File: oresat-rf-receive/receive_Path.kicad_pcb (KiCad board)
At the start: 4 copper layers, 26 x 60.3 mm, 32 parts, among them J1 Conn_Coaxial_142-0711-201, J2 0022232041, J3 0022232021, J5 0022232021, J6 Conn_Coaxial_142-0711-201, U1 TQP3M9037, U2 PAT1220-C-3DB, U3 SN74LVC1G32QDBVRQ1, U4 PAT1220-C-3DB, U5 TQP3M9037, U6 PD2328J5050S2HF, U7 LTC5505-1ES5

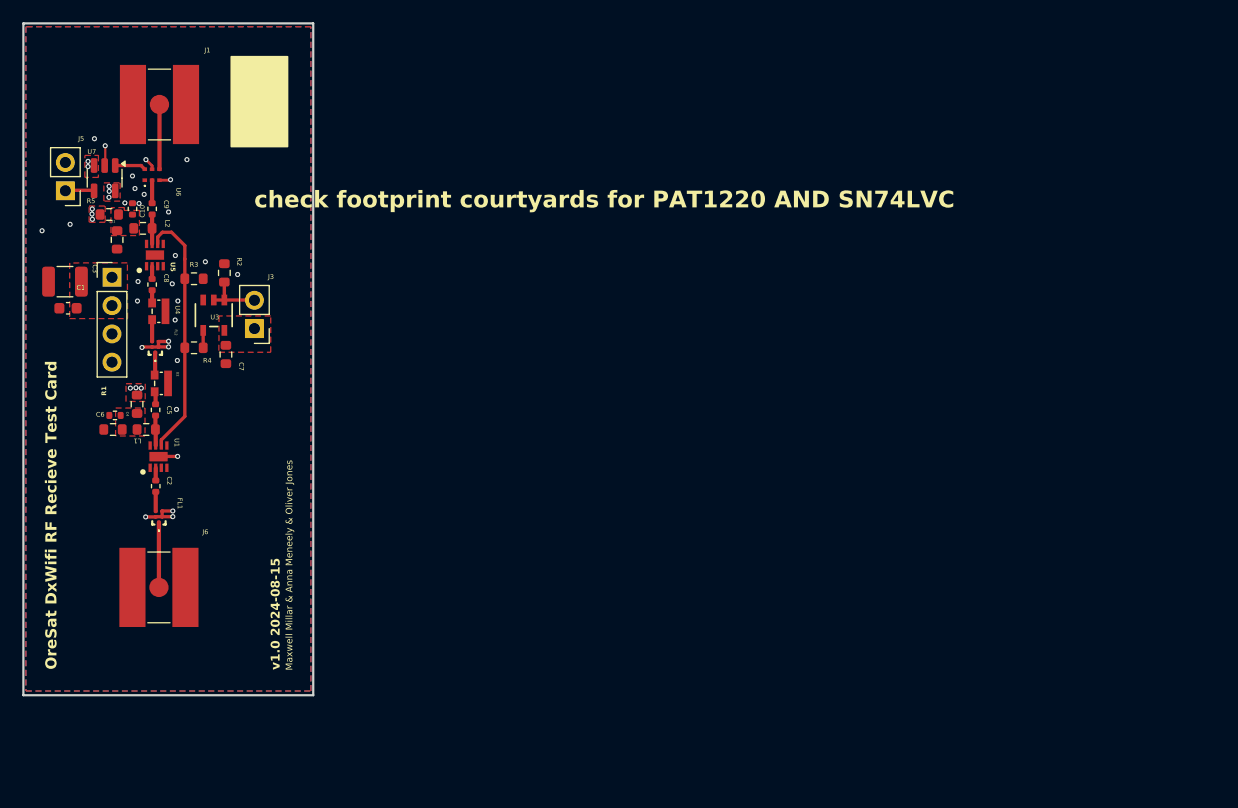
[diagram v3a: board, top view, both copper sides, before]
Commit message: 5V path changes and silkscreen descriptors update
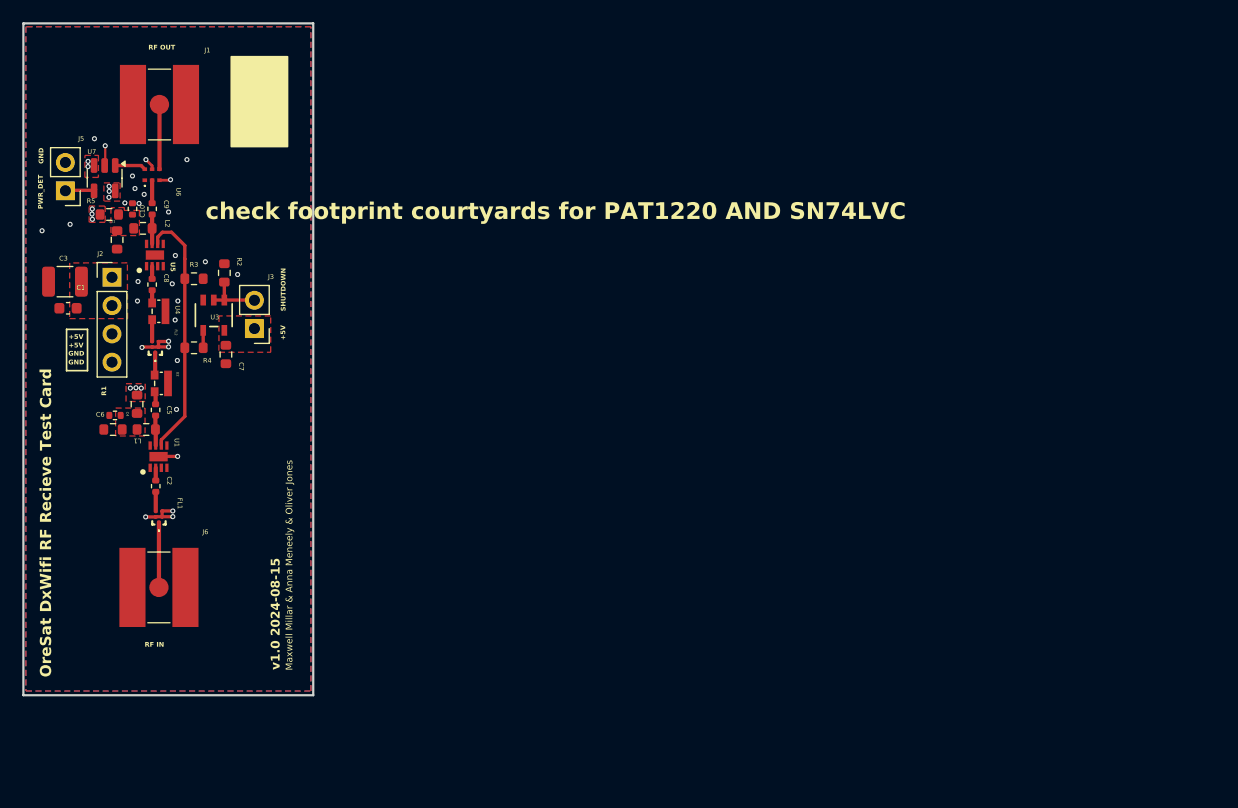
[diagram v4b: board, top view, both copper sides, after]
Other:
- board text added: "+5V"
- board text added: "GND"
- board text added: "PWR_DET"
- board text added: "RF IN"
- board text added: "RF OUT"
- board text added: "SHUTDOWN"
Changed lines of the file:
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@@
 		(tags "capacitor")
 		(property "Reference" "C3"
-			(at -2.69 1.1624 -90)
+			(at 0.1366 2.0928 0)
 			(unlocked yes)
 			(layer "F.SilkS")
@@
 		)
 		(property "Value" "22u"
-			(at 0 2.3 360)
+			(at 0 2.3 0)
 			(layer "F.Fab")
 			(hide yes)
@@
 		)
 		(property "Value" "2u2"
-			(at 0 1.43 360)
+			(at 0 1.43 0)
 			(layer "F.Fab")
 			(effects
@@
 		)
 		(fp_text user "${REFERENCE}"
-			(at 0 0 360)
+			(at 0 0 0)
 			(layer "F.Fab")
 			(effects
@@
 		(tags "Through hole pin header THT 1x04 2.54mm single row")
 		(property "Reference" "J2"
-			(at 0 -2.33 0)
+			(at -1.05675 -2.1111 0)
 			(unlocked yes)
 			(layer "F.SilkS")
-			(hide yes)
 			(effects
 				(font
@@
 		)
 		(property "Value" "15p"
-			(at 0 1.17 360)
+			(at 0 1.17 0)
 			(layer "F.Fab")
 			(effects
@@
 		)
 		(fp_text user "${REFERENCE}"
-			(at 0 0 360)
+			(at 0 0 0)
 			(layer "F.Fab")
 			(effects
@@
 	)
 	(gr_rect
+		(start 104.9528 110.9726)
+		(end 106.8324 114.681)
+		(stroke
+			(width 0.15)
+			(type default)
+		)
+		(fill none)
+		(layer "F.SilkS")
+	)
+	(gr_rect
 		(start 119.74413 86.491265)
 		(end 124.7902 94.559935)
@@
 		(layer "Edge.Cuts")
 	)
+	(gr_text "RF OUT"
+		(at 112.2934 85.9028 0)
+		(layer "F.SilkS")
+		(effects
+			(font
+				(size 0.425 0.425)
+				(thickness 0.075)
+				(bold yes)
+			)
+			(justify left bottom)
+		)
+	)
 	(gr_text "Maxwell Millar & Anna Meneely & Oliver Jones\n"
 		(at 125.2982 141.605 90)
@@
 		)
 	)
+	(gr_text "GND"
+		(at 105.1052 113.3856 0)
+		(layer "F.SilkS")
+		(effects
+			(font
+				(size 0.425 0.425)
+				(thickness 0.075)
+				(bold yes)
+			)
+			(justify left bottom)
+		)
+	)
+	(gr_text "PWR_DET"
+		(at 102.87 100.1776 90)
+		(layer "F.SilkS")
+		(effects
+			(font
+				(size 0.425 0.425)
+				(thickness 0.075)
+				(bold yes)
+			)
+			(justify left bottom)
+		)
+	)
 	(gr_text "OreSat DxWifi RF Recieve Test Card\n"
-		(at 104.1654 141.5288 90)
+		(at 103.6828 142.2146 90)
 		(layer "F.SilkS")
 		(effects
@@
 		)
 	)
+	(gr_text "+5V\n"
+		(at 124.6378 111.9378 90)
+		(layer "F.SilkS")
+		(effects
+			(font
+				(size 0.425 0.425)
+				(thickness 0.075)
+				(bold yes)
+			)
+			(justify left bottom)
+		)
+	)
 	(gr_text "v1.0 2024-08-15"
 		(at 124.1806 141.5542 90)
@@
 		)
 	)
+	(gr_text "+5V\n"
+		(at 105.1306 112.649 0)
+		(layer "F.SilkS")
+		(effects
+			(font
+				(size 0.425 0.425)
+				(thickness 0.075)
+				(bold yes)
+			)
+			(justify left bottom)
+		)
+	)
+	(gr_text "RF IN"
+		(at 111.9632 139.5222 0)
+		(layer "F.SilkS")
+		(effects
+			(font
+				(size 0.425 0.425)
+				(thickness 0.075)
+				(bold yes)
+			)
+			(justify left bottom)
+		)
+	)
 	(gr_text "${REVISION} ${ISSUE_DATE}"
 		(at 92.2528 126.1618 90)
@@
 		)
 	)
+	(gr_text "SHUTDOWN\n"
+		(at 124.6632 109.347 90)
+		(layer "F.SilkS")
+		(effects
+			(font
+				(size 0.425 0.425)
+				(thickness 0.075)
+				(bold yes)
+			)
+			(justify left bottom)
+		)
+	)
+	(gr_text "GND"
+		(at 105.1052 114.173 0)
+		(layer "F.SilkS")
+		(effects
+			(font
+				(size 0.425 0.425)
+				(thickness 0.075)
+				(bold yes)
+			)
+			(justify left bottom)
+		)
+	)
+	(gr_text "+5V\n"
+		(at 105.1306 111.887 0)
+		(layer "F.SilkS")
+		(effects
+			(font
+				(size 0.425 0.425)
+				(thickness 0.075)
+				(bold yes)
+			)
+			(justify left bottom)
+		)
+	)
+	(gr_text "GND"
+		(at 102.9208 96.1136 90)
+		(layer "F.SilkS")
+		(effects
+			(font
+				(size 0.425 0.425)
+				(thickness 0.075)
+				(bold yes)
+			)
+			(justify left bottom)
+		)
+	)
 	(gr_text "check footprint courtyards for PAT1220 AND SN74LVC"
-		(at 121.79555 100.2035 0)
+		(at 117.4242 101.2444 0)
 		(layer "F.SilkS")
 		(effects

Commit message: changed reference designators for rf inputs, added ground vias, adjusted text size for designators
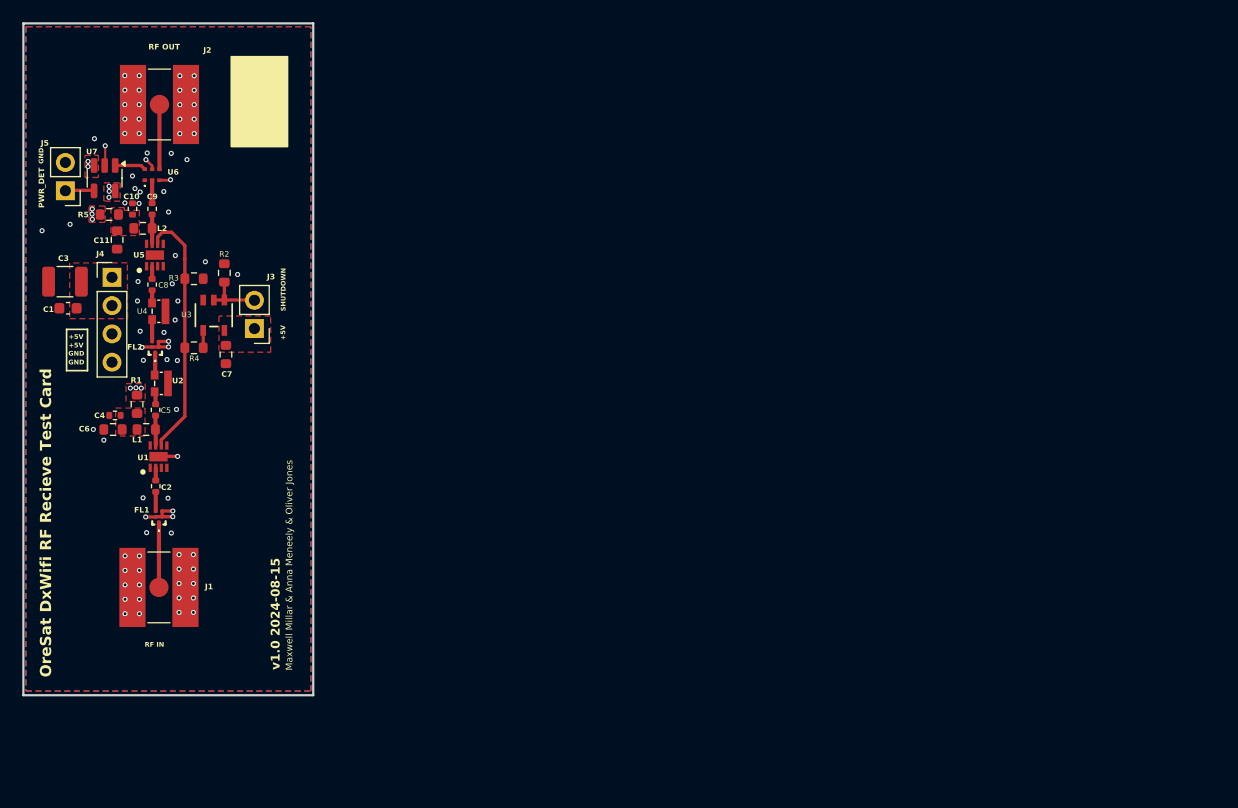
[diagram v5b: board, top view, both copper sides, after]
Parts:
- renumbered J6 to J1, J1 to J2, J2 to J4
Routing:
- net GND: vias 30 -> 83
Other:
- board text removed: "check footprint courtyards for PAT1220 AND SN74LVC"

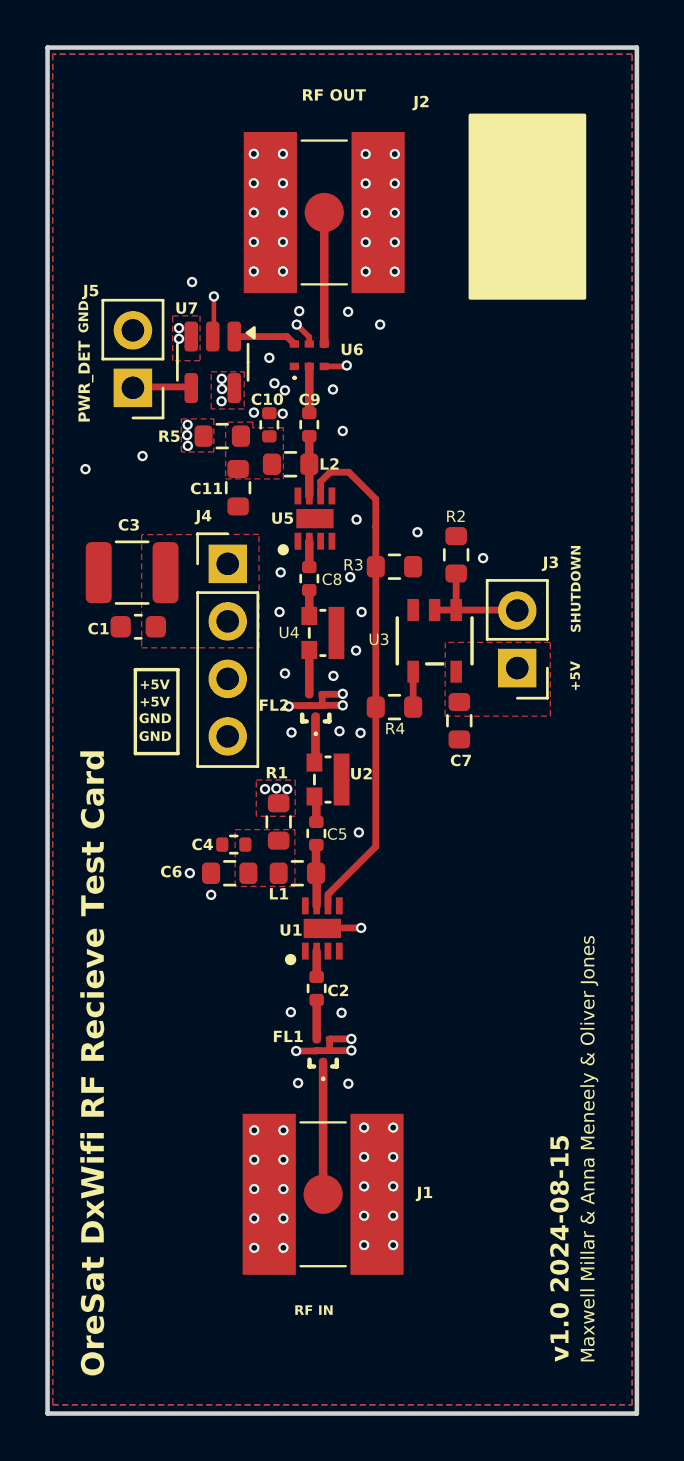
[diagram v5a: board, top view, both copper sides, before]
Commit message: Updated silkscreen, grounding, and Ref Des alignment
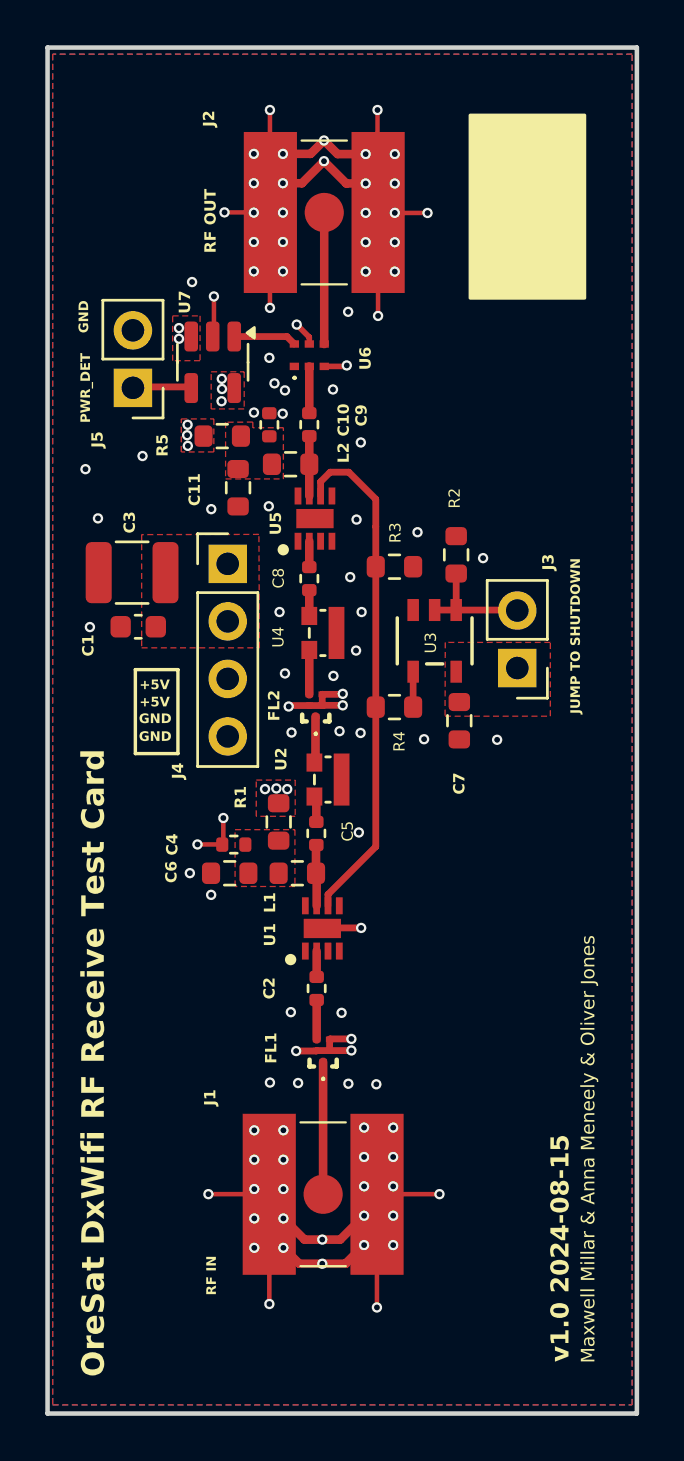
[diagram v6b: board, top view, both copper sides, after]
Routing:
- net GND: track 13.4 -> 70.5 mm, vias 83 -> 104
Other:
- board text added: "JUMP TO SHUTDOWN"
- board text added: "OreSat DxWifi RF Receive Test Card"
- board text removed: "OreSat DxWifi RF Recieve Test Card"
- board text removed: "SHUTDOWN"

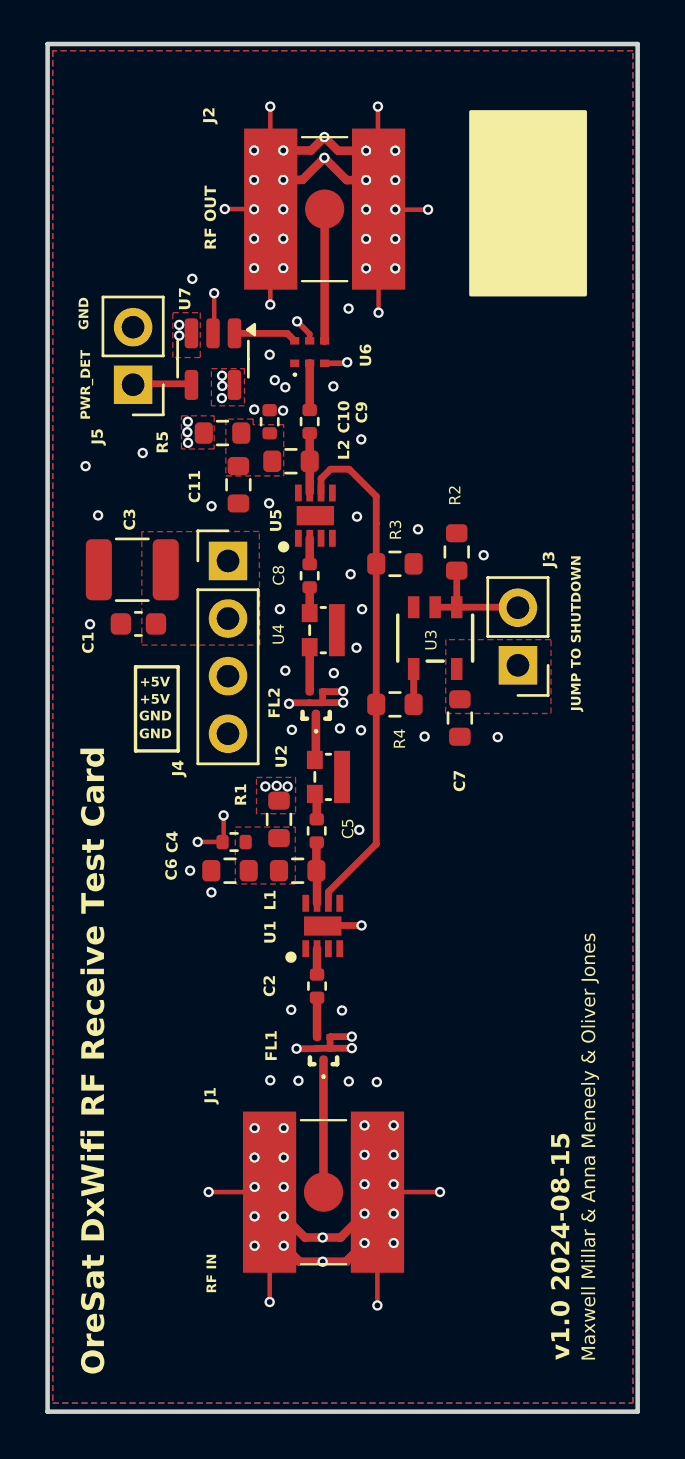
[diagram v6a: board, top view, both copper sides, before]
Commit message: edited silkscreen text and silkscreen in footprints
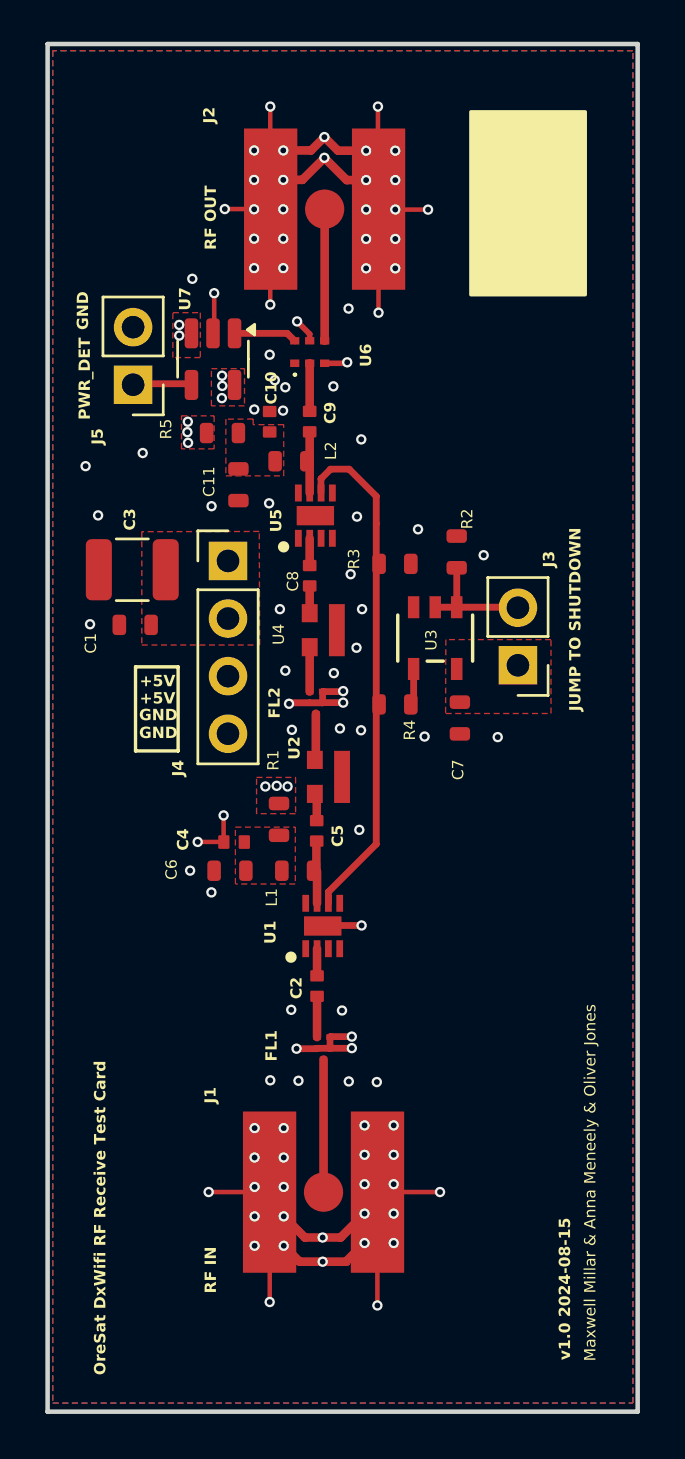
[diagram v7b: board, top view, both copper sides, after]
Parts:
- C1: footprint Capacitor_SMD:C_0603_1608Metric -> oresat-passives:0603-C-NOSILK
- C10, C2, C4, C5, C8, C9: footprint Resistor_SMD:R_0402_1005Metric -> oresat-passives:0402-C-NOSILK
- C11, C6, C7, L1, L2, R1, R2, R3, R4, R5: footprint Resistor_SMD:R_0603_1608Metric -> oresat-passives:0603-C-NOSILK
- moved C1 0.15 mm to (104.9, 109.1)
